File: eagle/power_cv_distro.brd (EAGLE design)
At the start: 101.6 x 80.6 mm, 11 parts, among them U1 POWER, U2 POWER, U3 POWER, U4 POWER, U5 POWER, U6 POWER, U7 POWER, U8 POWER, U9 POWER

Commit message: opamps
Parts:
- added R1, R2, R5, R6: 1k8, rcl:0204V
- added R3, R4, R8, R9: 1k, rcl:0207/7
- added U10, U11, U12, U13: TLV2372IP, Texas Instruments_By_element14_Batch_1:DIP254P762X508-8
- moved U3 45.5 mm to (53.3, 33.0)
- moved U5 39.8 mm to (94.0, 33.0)
- moved U2 36.4 mm to (64.8, 33.0)
- moved U8 35.3 mm to (15.2, 33.0)
- moved JP3 32.4 mm to (31.8, 69.8), turned to 0 degrees
- moved JP2 31.8 mm to (76.2, 72.4), turned to 0 degrees
- moved U9 31.1 mm to (17.8, 10.2), turned to 180 degrees
- moved U7 28.0 mm to (44.5, 33.0)
- moved U6 22.6 mm to (85.1, 33.0)
- moved U1 19.9 mm to (74.9, 33.0)
- moved U4 19.3 mm to (26.7, 33.0)
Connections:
- new net N$17: R1.2, U10.7, U6.13, U6.14
- new net N$18: R2.2, U10.1, U5.13, U5.14
- new net N$19: R1.1, R3.2, U10.6
- new net N$20: R2.1, R4.2, U10.2
- new net N$22: R6.2, U11.7, U2.13, U2.14
- new net N$23: R5.1, R9.2, U11.2
- new net N$24: R6.1, R8.2, U11.6
- new net N$26: R5.2, U1.13, U1.14, U11.1
- new net VDD: U12.8, U13.8
- net +12V: now also U10.8, U11.8
- net GND: now also R3.1, R4.1, R8.1, R9.1, U10.4, U11.4
- net N$2: now also U10.3; no longer U5.13, U5.14
- net N$4: now also U10.5; no longer U6.13, U6.14
- net N$6: now also U11.3; no longer U1.13, U1.14
- net N$8: now also U11.5; no longer U2.13, U2.14
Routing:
- net GND: track 34.6 -> 344.7 mm
- net +12V: track 120.7 -> 257.5 mm
- net -12V: track 129.3 -> 99.2 mm
- net VDD: track 0.00 -> 23.0 mm
- net N$22: track 0.00 -> 22.2 mm
- net N$17: track 0.00 -> 18.4 mm
- net N$18: track 0.00 -> 17.9 mm
- net N$26: track 0.00 -> 17.3 mm
- net N$3: track 19.1 -> 32.1 mm
- net N$1: track 21.4 -> 34.2 mm
- net N$16: track 23.0 -> 35.6 mm
- net N$15: track 19.7 -> 31.6 mm
- net N$8: track 24.5 -> 13.0 mm
- net N$5: track 19.9 -> 30.6 mm
- net N$24: track 0.00 -> 8.41 mm
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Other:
- board size 101.6 x 80.6 mm -> 100 x 80 mm

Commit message: opamps in
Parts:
- added R10, R13, R14, R7: 1k8, rcl:0204V
- added R11, R12, R15, R16: 1k, rcl:0207/7
- moved U12 33.7 mm to (41.9, 61.0), turned to 180 degrees
- moved U13 12.6 mm to (19.1, 61.0), turned to 180 degrees
- moved U9 4.07 mm to (15.2, 13.3)
- moved U4 3.81 mm to (30.5, 33.0)
- moved JP3 3.18 mm to (33.7, 72.4)
- moved U8 3.17 mm to (18.4, 33.0)
- moved U7 1.91 mm to (42.5, 33.0)
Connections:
- removed net VDD: U12.8, U13.8
- new net N$21: R11.2, R7.1, U12.2
- new net N$25: R10.1, R12.2, U12.6
- new net N$27: R7.2, U12.1, U3.13, U3.14
- new net N$28: R13.2, U13.1, U4.13, U4.14
- new net N$29: R14.2, U13.7, U8.13, U8.14
- new net N$30: JP3.3, U13.3
- new net N$31: R13.1, R15.2, U13.2
- new net N$32: R14.1, R16.2, U13.6
- net +12V: now also U12.8, U13.8
- net GND: now also R11.1, R12.1, R15.1, R16.1, U12.4, U13.4
- net N$10: now also U12.3; no longer U3.13, U3.14
- net N$12: now also U12.5; no longer U7.13, U7.14
- net N$14: now also R10.2, U12.7, U7.13, U7.14; no longer JP3.3, U4.13, U4.14
- net N$16: now also U13.5; no longer U8.13, U8.14
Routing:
- net GND: track 344.7 -> 461.7 mm
- net +12V: track 257.5 -> 304.1 mm
- net +5V: track 114.4 -> 157.0 mm
- net N$12: track 35.1 -> 0.00 mm
- net N$14: track 33.3 -> 0.00 mm
- net VDD: track 23.0 -> 0.00 mm
- net N$13: track 29.1 -> 42.3 mm
- net N$15: track 31.6 -> 43.1 mm
- net -12V: track 99.2 -> 106.9 mm
- net N$11: track 31.3 -> 38.0 mm
- net N$9: track 32.8 -> 35.5 mm

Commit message: placement
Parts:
- moved R16 109.4 mm to (22.9, 63.5), turned to 180 degrees
- moved R15 102.6 mm to (31.8, 59.7), turned to 270 degrees
- moved R12 94.3 mm to (45.7, 63.5), turned to 180 degrees
- moved R14 91.2 mm to (16.5, 57.1), turned to 270 degrees
- moved R11 90.9 mm to (54.6, 59.7), turned to 270 degrees
- moved R13 85.5 mm to (29.2, 54.6), turned to 270 degrees
- moved R10 76.7 mm to (39.4, 57.1), turned to 270 degrees
- moved R7 76.6 mm to (52.1, 54.6), turned to 270 degrees
- moved U9 48.3 mm to (6.99, 61.0), turned to 90 degrees
- moved U3 3.81 mm to (49.5, 33.0)
- moved U7 3.81 mm to (38.7, 33.0)
- moved U2 3.81 mm to (61.0, 33.0)
- moved U4 3.18 mm to (27.3, 33.0)
- moved R9 2.84 mm to (74.9, 59.7)
- moved U1 2.54 mm to (72.4, 33.0)
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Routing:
- net GND: track 461.7 -> 0.00 mm
- net +12V: track 304.1 -> 0.00 mm
- net +5V: track 157.0 -> 0.00 mm
- net -12V: track 106.9 -> 0.00 mm
- net N$15: track 43.1 -> 0.00 mm
- net N$13: track 42.3 -> 0.00 mm
- net N$11: track 38.0 -> 0.00 mm
- net N$10: track 36.2 -> 0.00 mm
- net N$16: track 35.9 -> 0.00 mm
- net N$9: track 35.5 -> 0.00 mm
- net N$1: track 34.2 -> 0.00 mm
- net N$3: track 32.1 -> 0.00 mm
- net N$7: track 32.0 -> 0.00 mm
- net N$5: track 30.6 -> 0.00 mm
- net N$2: track 24.7 -> 0.00 mm
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
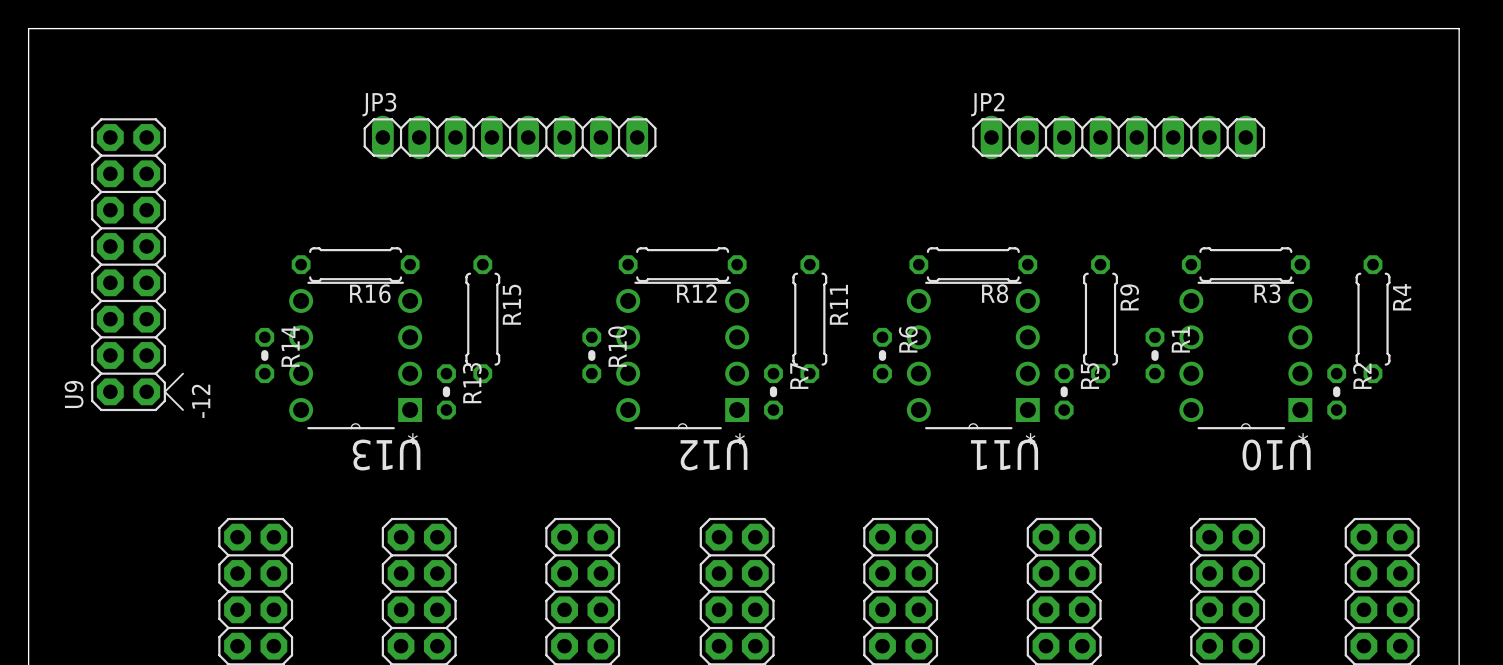
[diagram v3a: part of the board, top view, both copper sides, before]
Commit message: half routed
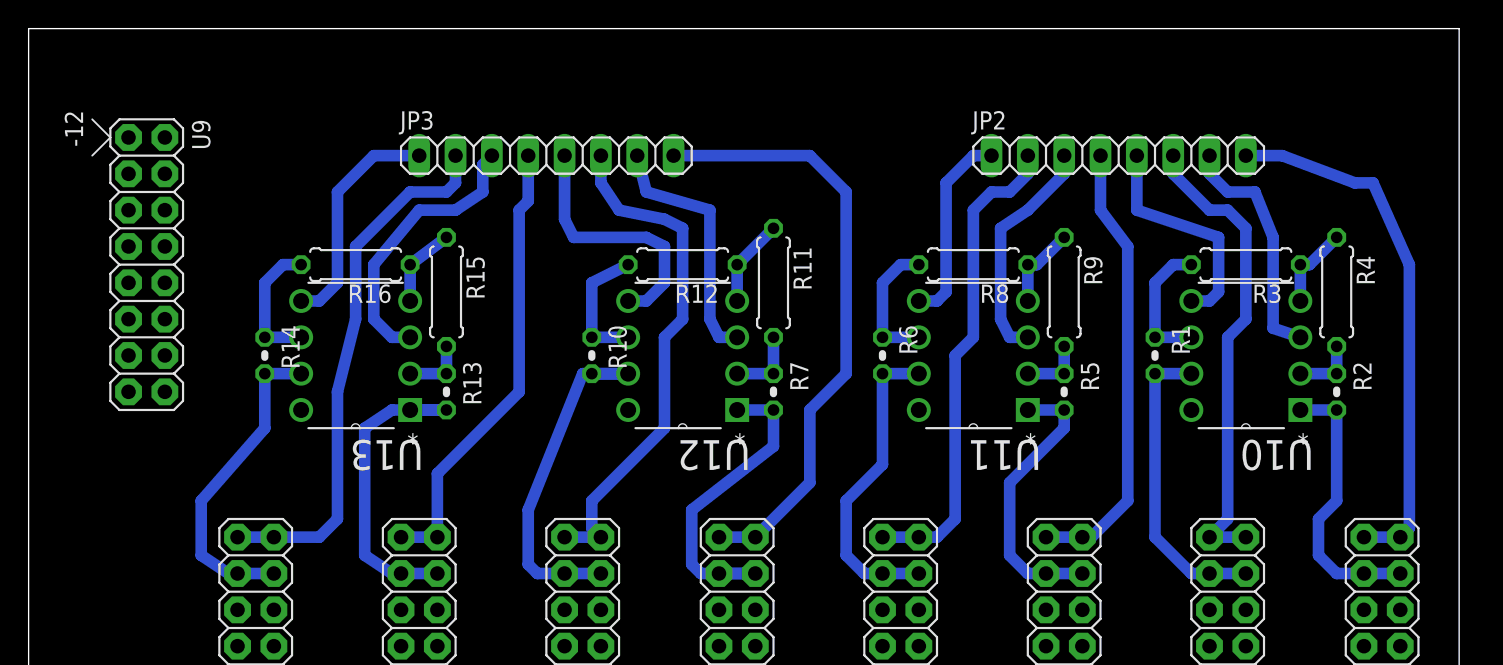
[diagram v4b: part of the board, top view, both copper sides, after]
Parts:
- moved U9 5.24 mm to (8.26, 66.0), turned to 270 degrees
- moved R11 3.59 mm to (52.1, 62.2)
- moved R4 3.18 mm to (91.4, 61.6)
- moved R9 3.18 mm to (72.4, 61.6)
- moved R15 3.18 mm to (29.2, 61.6)
- moved JP3 2.84 mm to (36.2, 71.1)
- moved JP2 1.27 mm to (76.2, 71.1)
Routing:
- net N$9: track 0.00 -> 42.4 mm
- net N$15: track 0.00 -> 37.4 mm
- net N$1: track 0.00 -> 37.3 mm
- net N$11: track 0.00 -> 35.9 mm
- net N$7: track 0.00 -> 33.9 mm
- net N$3: track 0.00 -> 33.1 mm
- net N$13: track 0.00 -> 31.8 mm
- net N$5: track 0.00 -> 31.5 mm
- net N$14: track 0.00 -> 25.1 mm
- net GND: track 0.00 -> 23.6 mm
- net N$27: track 0.00 -> 23.4 mm
- net N$28: track 0.00 -> 23.0 mm
- net N$29: track 0.00 -> 22.4 mm
- net N$22: track 0.00 -> 21.9 mm
- net N$17: track 0.00 -> 21.4 mm
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
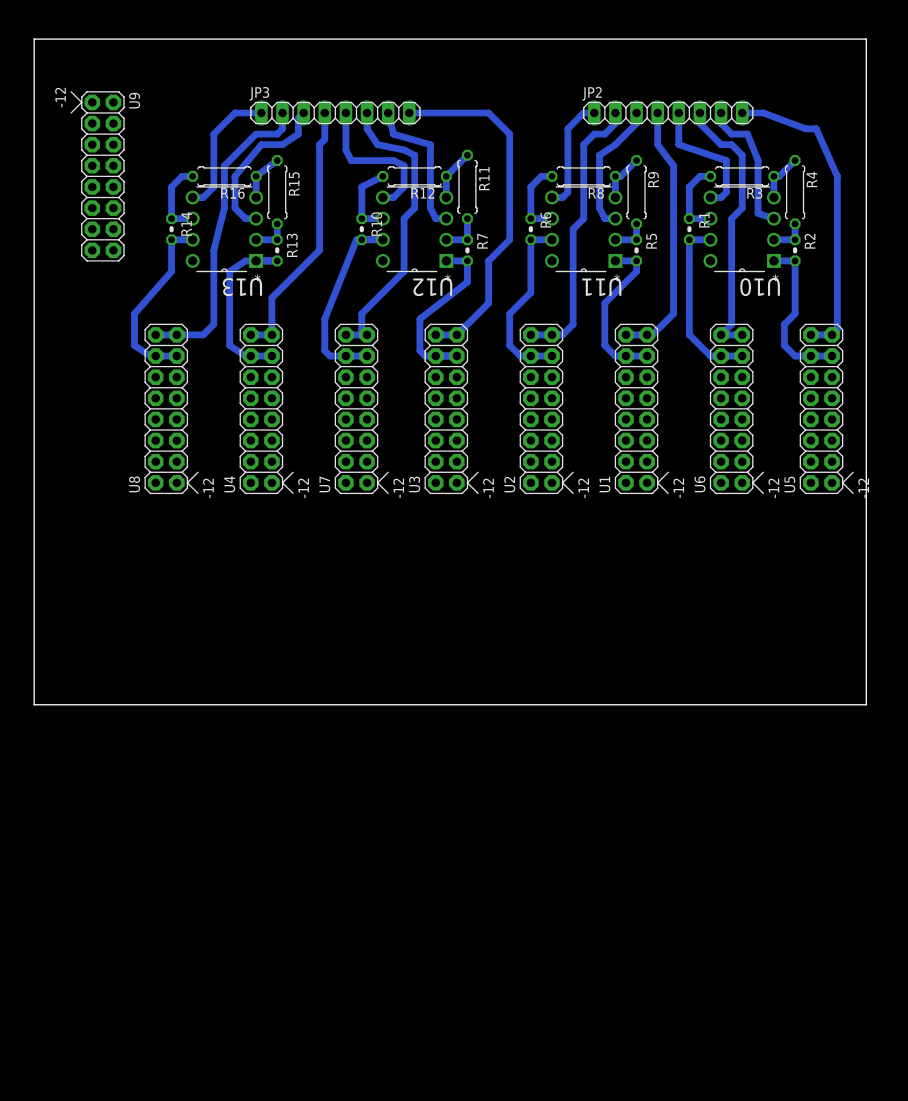
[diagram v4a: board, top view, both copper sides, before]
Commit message: output resistors
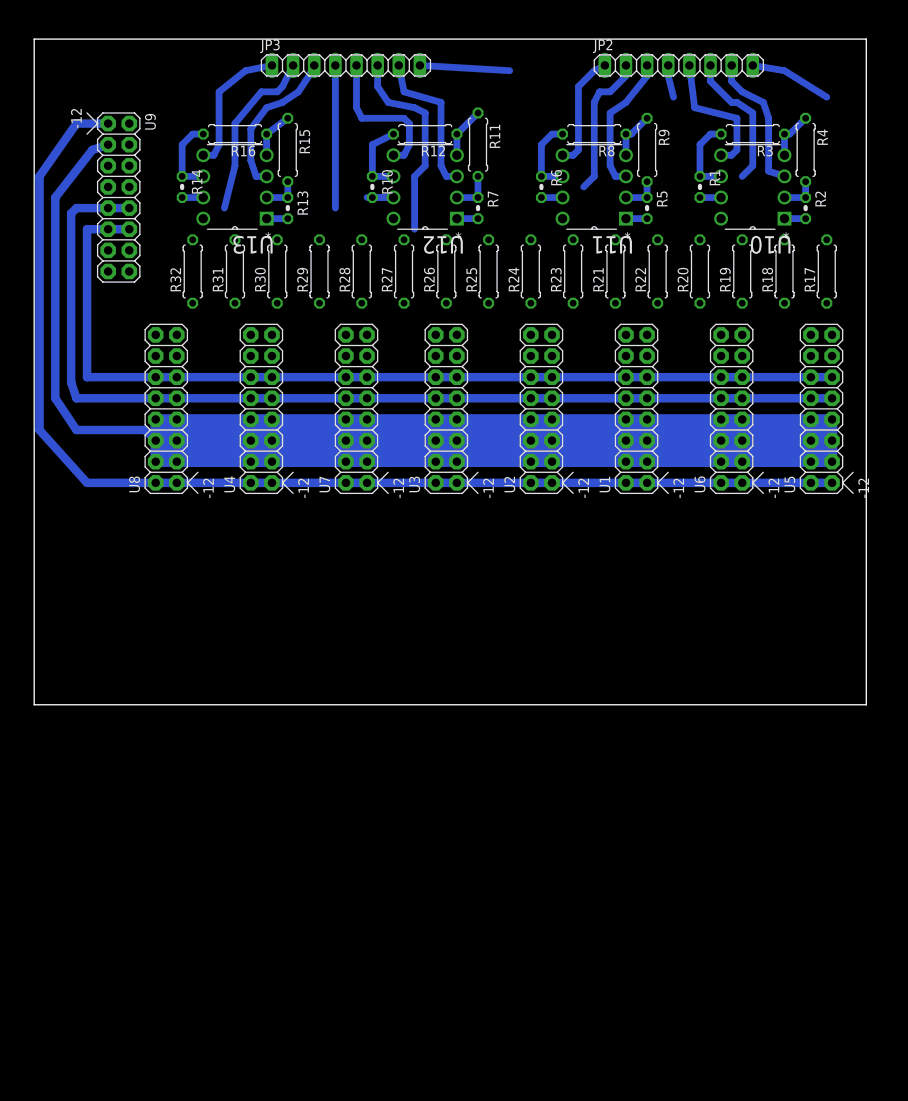
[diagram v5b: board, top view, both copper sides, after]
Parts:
- added R17, R18, R19, R20, R21, R22, R23, R24, R25, R26, R27, R28, R29, R30, R31, R32: 1k, rcl:0207/7
- moved JP3 5.85 mm to (37.5, 76.8)
- moved JP2 5.85 mm to (77.5, 76.8)
- moved R11 5.24 mm to (53.3, 67.3)
- moved U11 5.24 mm to (63.5, 66.0)
- moved U12 5.24 mm to (43.2, 66.0)
- moved U10 5.24 mm to (82.5, 66.0)
- moved U13 5.24 mm to (20.3, 66.0)
- moved R1 5.24 mm to (80.0, 62.2)
- moved R10 5.24 mm to (40.6, 62.2)
- moved R12 5.24 mm to (47.0, 68.6)
- moved R6 5.24 mm to (61.0, 62.2)
- moved R7 5.24 mm to (53.3, 59.7)
- moved R13 5.24 mm to (30.5, 59.7)
- moved R14 5.24 mm to (17.8, 62.2)
- moved R15 5.24 mm to (30.5, 66.7)
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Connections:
- new net N$33: R17.1, U5.15, U5.16
- new net N$34: R18.1, U5.13, U5.14
- new net N$35: R20.1, U6.13, U6.14
- new net N$36: R19.1, U6.15, U6.16
- new net N$37: R22.1, U1.15, U1.16
- new net N$38: R21.1, U1.13, U1.14
- new net N$39: R23.1, U2.15, U2.16
- new net N$40: R24.1, U2.13, U2.14
- new net N$41: R25.1, U3.15, U3.16
- new net N$42: R26.1, U3.13, U3.14
- new net N$43: R27.1, U7.15, U7.16
- new net N$44: R28.1, U7.13, U7.14
- new net N$45: R29.1, U4.15, U4.16
- new net N$46: R30.1, U4.13, U4.14
- new net N$47: R31.1, U8.15, U8.16
- new net N$48: R32.1, U8.13, U8.14
- net N$1: now also R17.2; no longer U5.15, U5.16
- net N$11: now also R27.2; no longer U7.15, U7.16
- net N$13: now also R29.2; no longer U4.15, U4.16
- net N$14: now also R28.2; no longer U7.13, U7.14
- net N$15: now also R31.2; no longer U8.15, U8.16
- net N$17: now also R20.2; no longer U6.13, U6.14
- net N$18: now also R18.2; no longer U5.13, U5.14
- net N$22: now also R24.2; no longer U2.13, U2.14
- net N$26: now also R21.2; no longer U1.13, U1.14
- net N$27: now also R26.2; no longer U3.13, U3.14
- net N$28: now also R30.2; no longer U4.13, U4.14
- net N$29: now also R32.2; no longer U8.13, U8.14
- net N$3: now also R19.2; no longer U6.15, U6.16
- net N$5: now also R22.2; no longer U1.15, U1.16
- net N$7: now also R23.2; no longer U2.15, U2.16
- net N$9: now also R25.2; no longer U3.15, U3.16
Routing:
- net -12V: track 0.00 -> 140.1 mm
- net +12V: track 0.00 -> 120.4 mm
- net +5V: track 0.00 -> 112.4 mm
- net GND: track 23.6 -> 71.6 mm
- net N$9: track 42.4 -> 10.8 mm
- net N$5: track 31.5 -> 3.89 mm
- net N$1: track 37.3 -> 9.85 mm
- net N$27: track 23.4 -> 2.54 mm
- net N$28: track 23.0 -> 2.54 mm
- net N$29: track 22.4 -> 2.54 mm
- net N$14: track 25.1 -> 5.71 mm
- net N$22: track 21.9 -> 2.54 mm
- net N$17: track 21.4 -> 2.54 mm
- net N$26: track 19.9 -> 2.54 mm
- net N$18: track 19.5 -> 2.54 mm
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
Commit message: routed
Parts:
- moved U5 4.02 mm to (95.9, 29.2)
- moved U6 4.02 mm to (85.1, 29.2)
- moved U7 4.02 mm to (40.0, 29.2)
- moved U4 4.02 mm to (28.6, 29.2)
- moved U8 4.02 mm to (17.1, 29.2)
- moved U1 4.02 mm to (73.7, 29.2)
- moved U2 4.02 mm to (62.2, 29.2)
- moved U3 4.02 mm to (50.8, 29.2)
- moved R11 0.64 mm to (53.3, 66.7)
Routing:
- net +12V: track 120.4 -> 227.0 mm
- net GND: track 71.6 -> 172.9 mm, vias 0 -> 8
- net N$48: track 0.00 -> 20.3 mm
- net N$9: track 10.8 -> 29.7 mm
- net N$5: track 3.89 -> 22.1 mm
- net N$46: track 0.00 -> 18.1 mm
- net N$40: track 0.00 -> 17.2 mm
- net N$1: track 9.85 -> 27.0 mm
- net N$44: track 0.00 -> 16.8 mm
- net N$38: track 0.00 -> 15.9 mm
- net N$42: track 0.00 -> 15.9 mm
- net N$35: track 0.00 -> 15.3 mm
- net N$34: track 0.00 -> 15.2 mm
- net N$47: track 0.00 -> 13.7 mm
- net N$45: track 0.00 -> 12.5 mm
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
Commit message: route tweaked
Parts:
- added C1, C2, C3, C4: (no value), rcl:C025-025X050
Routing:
- net -12V: track 147.7 -> 144.9 mm
- net N$1: track 27.0 -> 26.1 mm
- net GND: track 172.9 -> 172.1 mm
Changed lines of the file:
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@@
 <element name="R31" library="rcl" package="0207/7" value="1k" x="24.13" y="52.07" rot="R90"/>
 <element name="R32" library="rcl" package="0207/7" value="1k" x="19.05" y="52.07" rot="R90"/>
+<element name="C1" library="rcl" package="C025-025X050" value="" x="3.81" y="-3.81"/>
+<element name="C2" library="rcl" package="C025-025X050" value="" x="3.81" y="-8.89"/>
+<element name="C3" library="rcl" package="C025-025X050" value="" x="3.81" y="-13.97"/>
+<element name="C4" library="rcl" package="C025-025X050" value="" x="3.81" y="-19.05"/>
 </elements>
 <signals>
 <signal name="N$1">
 <contactref element="JP2" pad="8"/>
-<wire x1="86.36" y1="76.835" x2="90.17" y2="76.2" width="0.8128" layer="16"/>
-<wire x1="90.17" y1="76.2" x2="95.25" y2="73.025" width="0.8128" layer="16"/>
+<wire x1="86.36" y1="76.835" x2="90.17" y2="74.93" width="0.8128" layer="16"/>
+<wire x1="90.17" y1="74.93" x2="95.25" y2="71.755" width="0.8128" layer="16"/>
 <contactref element="R17" pad="2"/>
-<wire x1="95.25" y1="73.025" x2="95.25" y2="55.88" width="0.8128" layer="16"/>
+<wire x1="95.25" y1="71.755" x2="95.25" y2="55.88" width="0.8128" layer="16"/>
 </signal>
 <signal name="N$2">
@@
 <wire x1="6.985" y1="66.675" x2="2.54" y2="60.96" width="1.016" layer="16"/>
 <wire x1="2.54" y1="60.96" x2="2.54" y2="33.02" width="1.016" layer="16"/>
-<wire x1="2.54" y1="33.02" x2="5.08" y2="29.21" width="1.016" layer="16"/>
-<wire x1="5.08" y1="29.21" x2="14.605" y2="29.21" width="1.016" layer="16"/>
+<wire x1="2.54" y1="33.02" x2="7.62" y2="29.21" width="1.016" layer="16"/>
+<wire x1="7.62" y1="29.21" x2="14.605" y2="29.21" width="1.016" layer="16"/>
 <wire x1="14.605" y1="29.21" x2="15.875" y2="27.94" width="1.016" layer="16"/>
 <wire x1="8.89" y1="64.77" x2="8.89" y2="62.23" width="0.8128" layer="16"/>
@@
 <contactref element="U9" pad="1"/>
 <contactref element="U9" pad="2"/>
-<wire x1="8.89" y1="69.85" x2="5.08" y2="69.85" width="1.016" layer="16"/>
-<wire x1="5.08" y1="69.85" x2="0.635" y2="63.5" width="1.016" layer="16"/>
-<wire x1="0.635" y1="63.5" x2="0.635" y2="29.21" width="1.016" layer="16"/>
-<wire x1="0.635" y1="29.21" x2="6.35" y2="22.86" width="1.016" layer="16"/>
-<wire x1="6.35" y1="22.86" x2="15.875" y2="22.86" width="1.016" layer="16"/>
+<wire x1="8.89" y1="69.85" x2="6.35" y2="69.85" width="1.016" layer="16"/>
+<wire x1="6.35" y1="69.85" x2="0.635" y2="62.23" width="1.016" layer="16"/>
+<wire x1="0.635" y1="62.23" x2="0.635" y2="31.75" width="1.016" layer="16"/>
+<wire x1="0.635" y1="31.75" x2="10.795" y2="22.86" width="1.016" layer="16"/>
+<wire x1="10.795" y1="22.86" x2="15.875" y2="22.86" width="1.016" layer="16"/>
 <wire x1="15.875" y1="22.86" x2="97.155" y2="22.86" width="1.016" layer="16"/>
 <wire x1="97.155" y1="22.86" x2="94.615" y2="22.86" width="0" layer="19" extent="1-1"/>
@@
 <wire x1="8.89" y1="59.69" x2="5.08" y2="59.69" width="1.016" layer="16"/>
 <wire x1="5.08" y1="59.69" x2="4.445" y2="59.055" width="1.016" layer="16"/>
-<wire x1="4.445" y1="59.055" x2="4.445" y2="34.925" width="1.016" layer="16"/>
-<wire x1="4.445" y1="34.925" x2="5.08" y2="33.02" width="1.016" layer="16"/>
-<wire x1="5.08" y1="33.02" x2="15.875" y2="33.02" width="1.016" layer="16"/>
+<wire x1="4.445" y1="59.055" x2="4.445" y2="34.29" width="1.016" layer="16"/>
+<wire x1="4.445" y1="34.29" x2="6.985" y2="33.02" width="1.016" layer="16"/>
+<wire x1="6.985" y1="33.02" x2="15.875" y2="33.02" width="1.016" layer="16"/>
 <wire x1="15.875" y1="33.02" x2="97.155" y2="33.02" width="1.016" layer="16"/>
 <wire x1="8.89" y1="59.69" x2="11.43" y2="59.69" width="1.016" layer="16"/>

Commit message: cutout
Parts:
- C1, C2, C3, C4: value (none) -> 100n
- moved C4 125.8 mm to (95.2, 67.3), turned to 90 degrees
- moved C3 108.4 mm to (75.6, 67.3), turned to 90 degrees
- moved C2 91.9 mm to (55.2, 67.3), turned to 90 degrees
- moved C1 76.9 mm to (33.0, 67.3), turned to 90 degrees
- moved R23 1.27 mm to (66.0, 52.1)
- moved R25 1.27 mm to (55.9, 52.1)
- moved R29 1.27 mm to (35.6, 52.1)
- moved R31 1.27 mm to (25.4, 52.1)
- moved R17 1.27 mm to (96.5, 52.1)
- moved R19 1.27 mm to (86.4, 52.1)
- moved R22 1.27 mm to (76.2, 52.1)
- moved R27 1.27 mm to (45.7, 52.1)
- moved R11 0.64 mm to (52.7, 66.7)
- moved R12 0.64 mm to (46.4, 68.6)
- moved R7 0.64 mm to (52.7, 59.7)
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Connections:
- net +12V: now also C1.1, C2.1, C3.1, C4.1
- net GND: now also C1.2, C2.2, C3.2, C4.2
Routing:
- net +12V: track 226.6 -> 296.7 mm
- net GND: track 172.1 -> 185.4 mm
- net N$14: track 11.1 -> 7.88 mm
- net N$48: track 20.3 -> 18.2 mm
- net N$1: track 26.1 -> 28.0 mm
- net N$11: track 25.8 -> 24.4 mm
- net N$46: track 18.1 -> 17.0 mm
- net N$9: track 29.7 -> 30.8 mm
- net N$10: track 18.2 -> 17.3 mm
- net N$40: track 17.2 -> 16.3 mm
- net N$42: track 15.9 -> 15.1 mm
- net N$8: track 13.7 -> 14.5 mm
- net N$44: track 16.8 -> 16.0 mm
- net N$24: track 9.42 -> 8.83 mm
- net N$7: track 23.7 -> 23.2 mm
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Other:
- board size 100 x 80 mm -> 101.6 x 80 mm
